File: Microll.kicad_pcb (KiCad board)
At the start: 2 copper layers, 39 x 46 mm, 33 parts, among them J1 Conn_01x12, J2 Conn_02x10_Top_Bottom, J3 Conn_01x08, J6 USB_C_Receptacle_USB2.0_16P, SW4 SW_DIP_x03, U1 ESP32-C3-WROOM-02-N4, U2 TLV76733DRVx, U3 STM32G0B1CBU6, U4 USBLC6-2P6, U5 DPDT_Switch_x2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

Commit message: Completed Microll V1.0
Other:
- board text added: "5V"
- board text added: "ADC1_IN0"
- board text added: "ADC1_IN1"
- board text added: "BOOT"
- board text added: "DAC1"
- board text added: "EN"
- board text added: "ESP32"
- board text added: "MISO"
- board text added: "MOSI"
- board text added: "Microll V1.0"
- board text added: "PA2"
- board text added: "PA3"
- board text added: "PA8"
- board text added: "PB0"
- board text added: "PB1"
- board text added: "PB13"
- board text added: "PB14"
- board text added: "PB15"
- board text added: "RESET"
- board text added: "SCK"
- board text added: "STM32"
- board text added: "U_RX"
- board text added: "U_TX"
- board text added: "V_IN"
- board text removed: "Remember to break out these 4 pins"

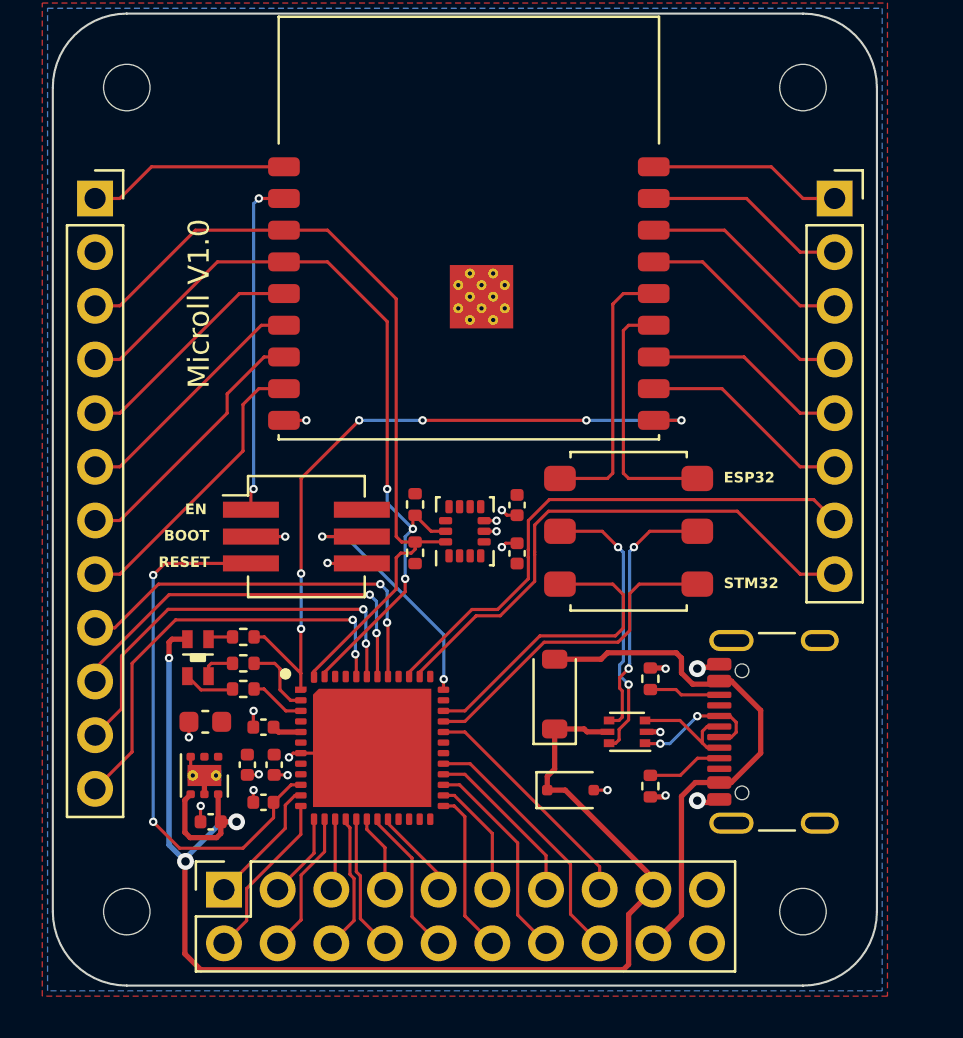
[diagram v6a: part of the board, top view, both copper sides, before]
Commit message: SWDIO and SWCLK now accessible through gpio pins. Microcontroller changed to more solder friendly package
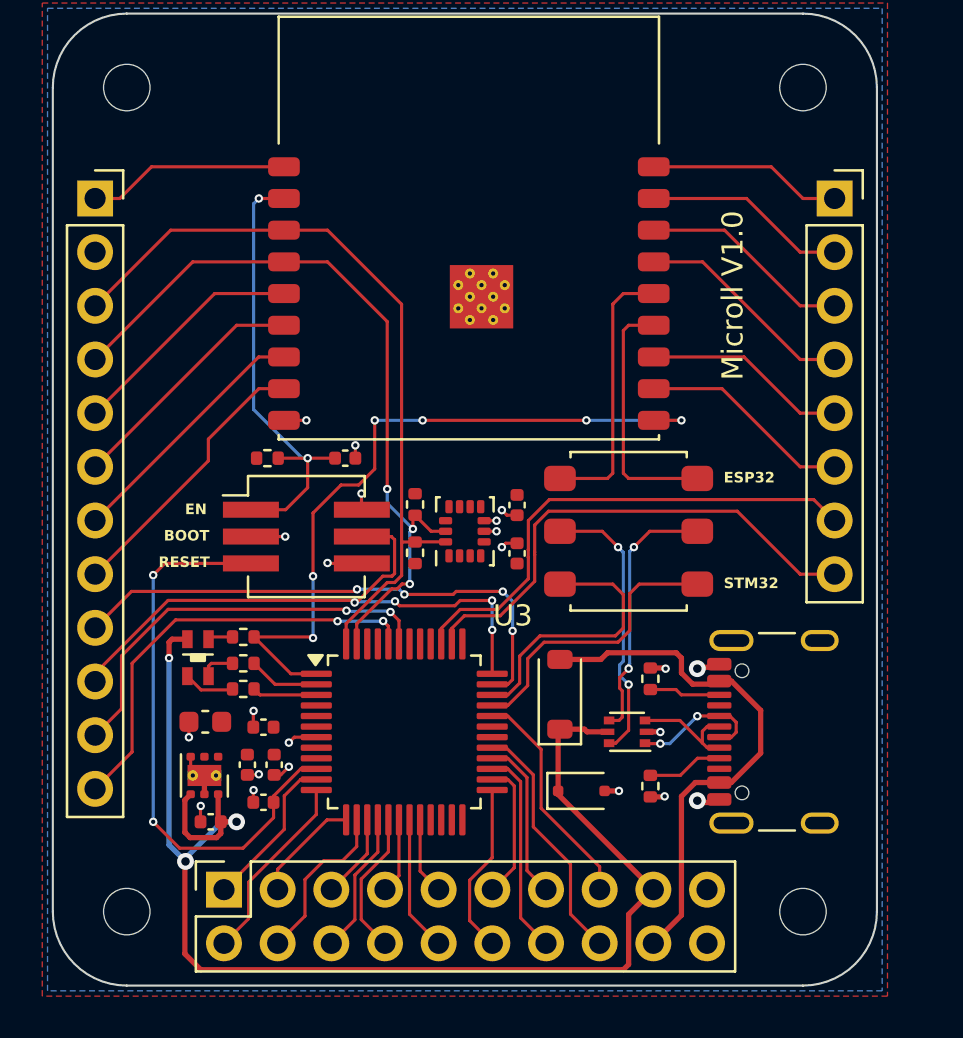
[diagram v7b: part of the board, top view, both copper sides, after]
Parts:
- added C9: 1uF, Capacitor_SMD:C_0402_1005Metric, F.Cu at (100.8, 66.0)
- added R8: 10k, Resistor_SMD:R_0402_1005Metric, F.Cu at (97.2, 66.0)
- U3: value STM32G0B1CBU6 -> STM32G0B1CBT6; footprint STM32:STM32G0B1CBU6 -> Package_QFP:LQFP-48_7x7mm_P0.5mm
- moved U3 1.70 mm to (103.6, 79.0)
- moved D3 0.52 mm to (112.0, 81.8)
- moved D2 0.25 mm to (111.0, 77.2)
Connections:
- J1 pad 10: /PB3 -> /BOOT
- J1 pad 9: /PD3 -> /PA13
- SW4 pad 6: +3.3V -> GND
- U3 pad 35: unconnected-(U3-PA13-Pad35) -> /PA13
- U3 pad 41: /PD3 -> unconnected-(U3-PD3-Pad41)
- U3 pad 42: /PB3 -> unconnected-(U3-PB3-Pad42)
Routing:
- net /PA13: track 0.00 -> 25.6 mm, vias 0 -> 4
- net /PB3: track 19.1 -> 0.00 mm, vias 2 -> 0
- net /PD3: track 18.9 -> 0.00 mm, vias 2 -> 0
- net /BOOT: track 12.2 -> 30.0 mm, vias 2 -> 4
- net /EN: track 16.1 -> 22.0 mm
- net SDA: track 39.4 -> 36.9 mm
- net STM32_USB-: track 15.7 -> 13.9 mm
- net STM32_USB+: track 14.9 -> 13.0 mm
- net CAN_TX: track 25.8 -> 23.9 mm
- net CAN_RX: track 25.8 -> 24.0 mm
- net SCL: track 38.4 -> 36.6 mm
- net +3.3V: track 10.9 -> 9.56 mm
- net /ADC1_IN0: track 6.13 -> 7.46 mm
- net /RESET: track 25.7 -> 26.9 mm
- net GND: track 22.0 -> 20.9 mm, vias 20 -> 22
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
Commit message: Made Microll V2 and updated Gerber Files
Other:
- board text added: "Microll V2"
- board text added: "© Ruben Trovoada"
- board text removed: "Microll V1.0"
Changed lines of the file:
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@@
 		)
 		(property "Value" "1uF"
-			(at 0 1.16 360)
+			(at 0 1.16 0)
 			(layer "F.Fab")
 			(effects
@@
 		)
 		(fp_text user "${REFERENCE}"
-			(at 0 0 360)
+			(at 0 0 0)
 			(layer "F.Fab")
 			(effects
@@
 		)
 		(property "Value" "10k"
-			(at 0 1.17 360)
+			(at 0 1.17 0)
 			(layer "F.Fab")
 			(effects
@@
 		)
 		(fp_text user "${REFERENCE}"
-			(at 0 0 360)
+			(at 0 0 0)
 			(layer "F.Fab")
 			(effects
@@
 		)
 	)
+	(gr_text "© Ruben Trovoada"
+		(at 114.3 48.8442 0)
+		(layer "B.SilkS")
+		(effects
+			(font
+				(size 1 1)
+				(thickness 0.15)
+			)
+			(justify left bottom mirror)
+		)
+	)
 	(gr_text "3.3V"
 		(at 94.25 54.5 0)
@@
 		)
 	)
-	(gr_text "Microll V1.0"
-		(at 119.761 62.357 90)
+	(gr_text "Microll V2"
+		(at 120.2182 64.008 90)
 		(layer "F.SilkS")
 		(effects
